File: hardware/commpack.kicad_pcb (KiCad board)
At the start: 2 copper layers, 103.8 x 62.5 mm, 11 parts, among them J1 1240COMM, J2 1240COMM_EXT, J3 L8BE-1G1T-91A

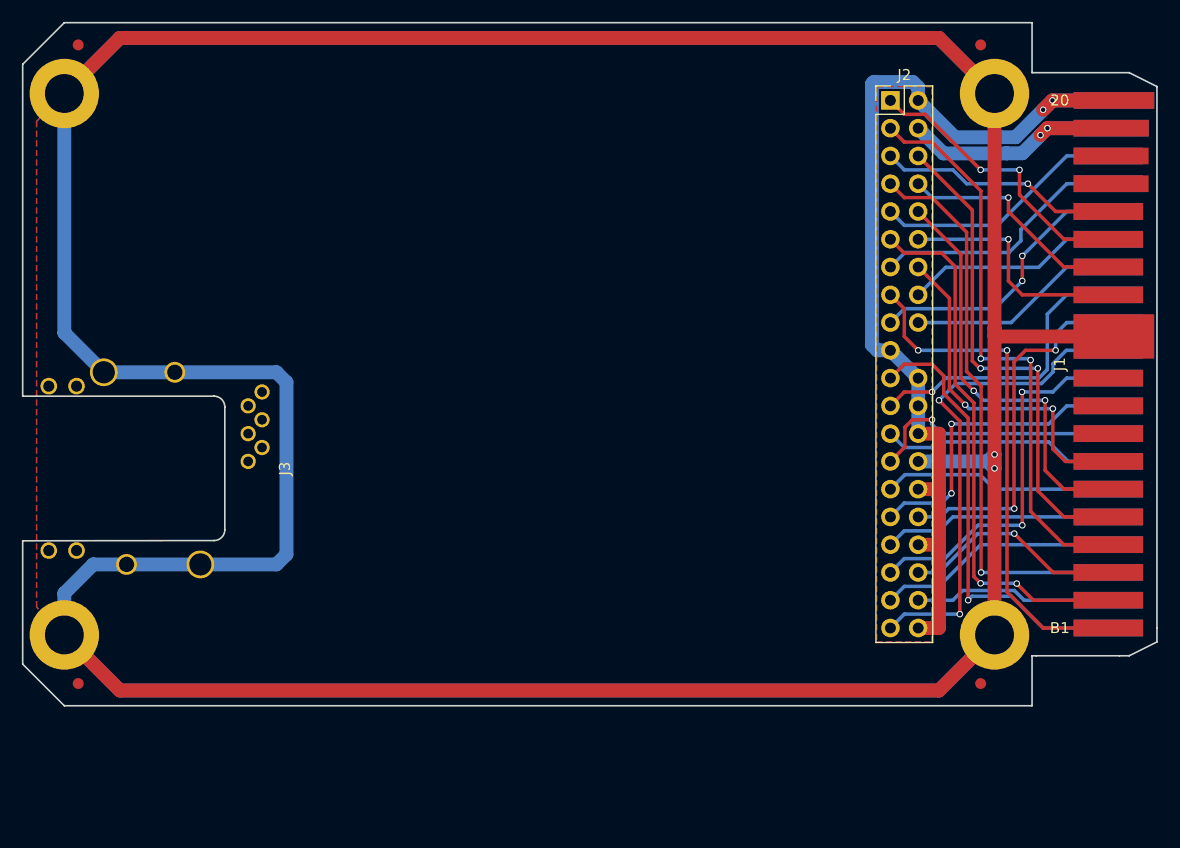
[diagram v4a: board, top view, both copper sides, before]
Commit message: Place UART and ROM, route data bus.
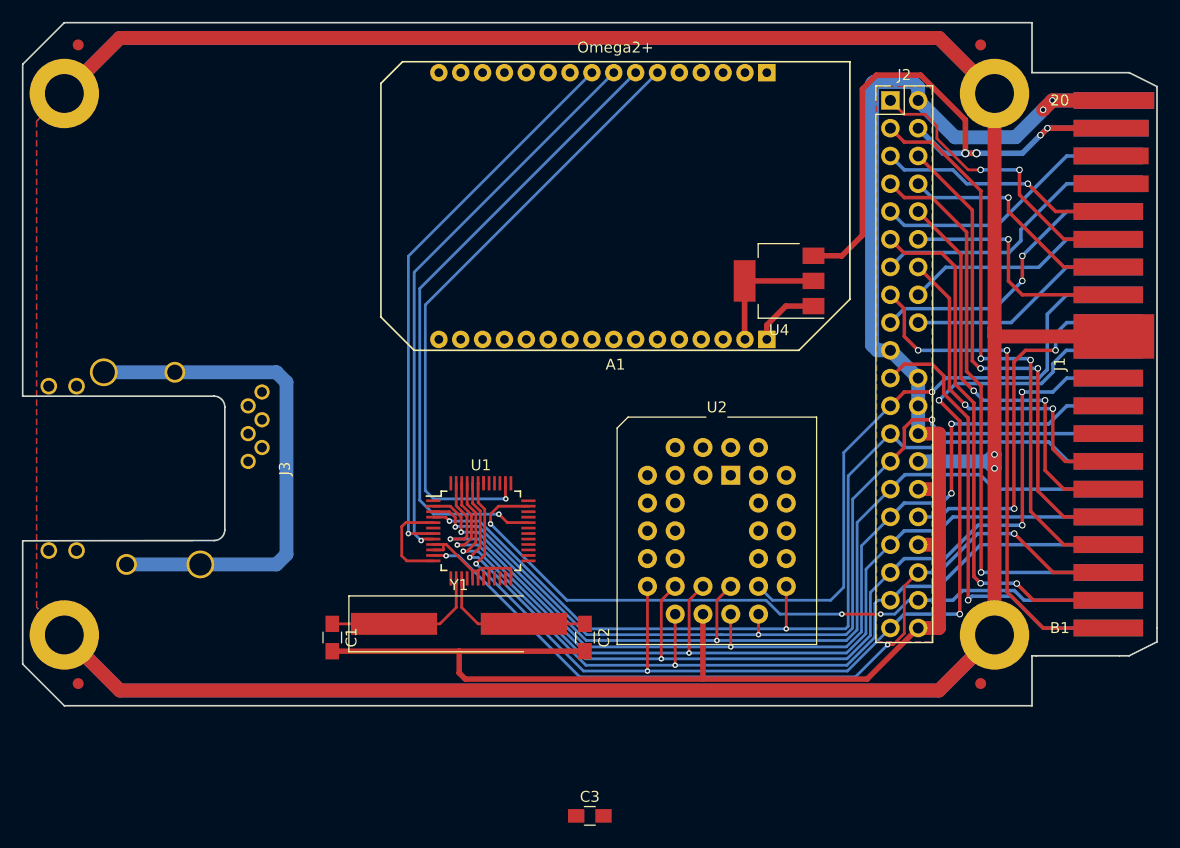
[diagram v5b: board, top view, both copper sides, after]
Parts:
- added A1: Omega2+, ether1240:Omega2, F.Cu at (176.1, 74.4)
- added C1: 22u, Capacitors_SMD:C_0805_HandSoldering, F.Cu at (150.2, 113.9)
- added C2: 22u, Capacitors_SMD:C_0805_HandSoldering, F.Cu at (173.4, 113.9)
- added C3: 22u, Capacitors_SMD:C_0805_HandSoldering, F.Cu at (173.8, 130.2)
- added U1: SC16C550B, Housings_QFP:LQFP-48_7x7mm_Pitch0.5mm, F.Cu at (163.8, 104.1)
- added U2: SST39SF010A, ether1240:PLCC-32_THT-Socket, F.Cu at (186.7, 99.1)
- added U4: AP1117-33, TO_SOT_Packages_SMD:SOT-223-3_TabPin2, F.Cu at (191.1, 81.3)
- added Y1: Crystal, Crystals:Crystal_SMD_HC49-SD_HandSoldering, F.Cu at (161.8, 112.6)
- J1: footprint 1240COMM -> ether1240:1240COMM
- J3: footprint L8BE-1G1T-91A -> ether1240:L8BE-1G1T-91A
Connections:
- net +5V renamed VCC
- net Net-(J1-PadA12) renamed /H-FREQ
- J1 pad B10: Net-(J1-PadB10) -> (no net)
- J1 pad B17: Net-(J1-PadB17) -> (no net)
- J1 pad B18: Net-(J1-PadB18) -> (no net)
- J1 pad B8: Net-(J1-PadB8) -> (no net)
- J1 pad B9: Net-(J1-PadB9) -> (no net)
- J3 pad 11: Net-(J3-Pad11) -> (no net)
- J3 pad 5: Net-(J3-Pad5) -> (no net)
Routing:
- net GND: track 85.7 -> 180.6 mm
- net /H-D7: track 18.2 -> 83.6 mm, vias 0 -> 2
- net /H-D3: track 17.8 -> 82.7 mm, vias 0 -> 2
- net /H-D5: track 17.9 -> 82.6 mm, vias 0 -> 2
- net /H-D4: track 24.7 -> 88.4 mm, vias 2 -> 4
- net /H-D2: track 31.3 -> 94.4 mm, vias 2 -> 4
- net /H-D6: track 20.2 -> 82.5 mm, vias 1 -> 3
- net /H-D0: track 41.9 -> 101.2 mm, vias 2 -> 4
- net /H-D1: track 18.9 -> 77.9 mm, vias 0 -> 2
- net /A-~CTS: track 0.00 -> 58.1 mm, vias 0 -> 1
- net /A-~RTS: track 0.00 -> 56.2 mm, vias 0 -> 1
- net /H-~CS: track 17.2 -> 73.2 mm, vias 1 -> 3
- net /A-RX: track 0.00 -> 51.8 mm, vias 0 -> 1
- net /A-TX: track 0.00 -> 51.4 mm, vias 0 -> 1
- net /H-RST: track 15.0 -> 63.3 mm, vias 0 -> 3
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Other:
- net class Default: clearance 0.2 -> 0.1524; trace_width 0.32258 -> 0.254; via_dia 0.6 -> 0.508; via_drill 0.4 -> 0.254
- net class Power: clearance 0.2 -> 0.1524; trace_width 1.27 -> 0.508; via_dia 0.6 -> 0.762; via_drill 0.4 -> 0.508
- rule trace_clearance: 0.2 -> 0.1524

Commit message: Route the remaining signals.
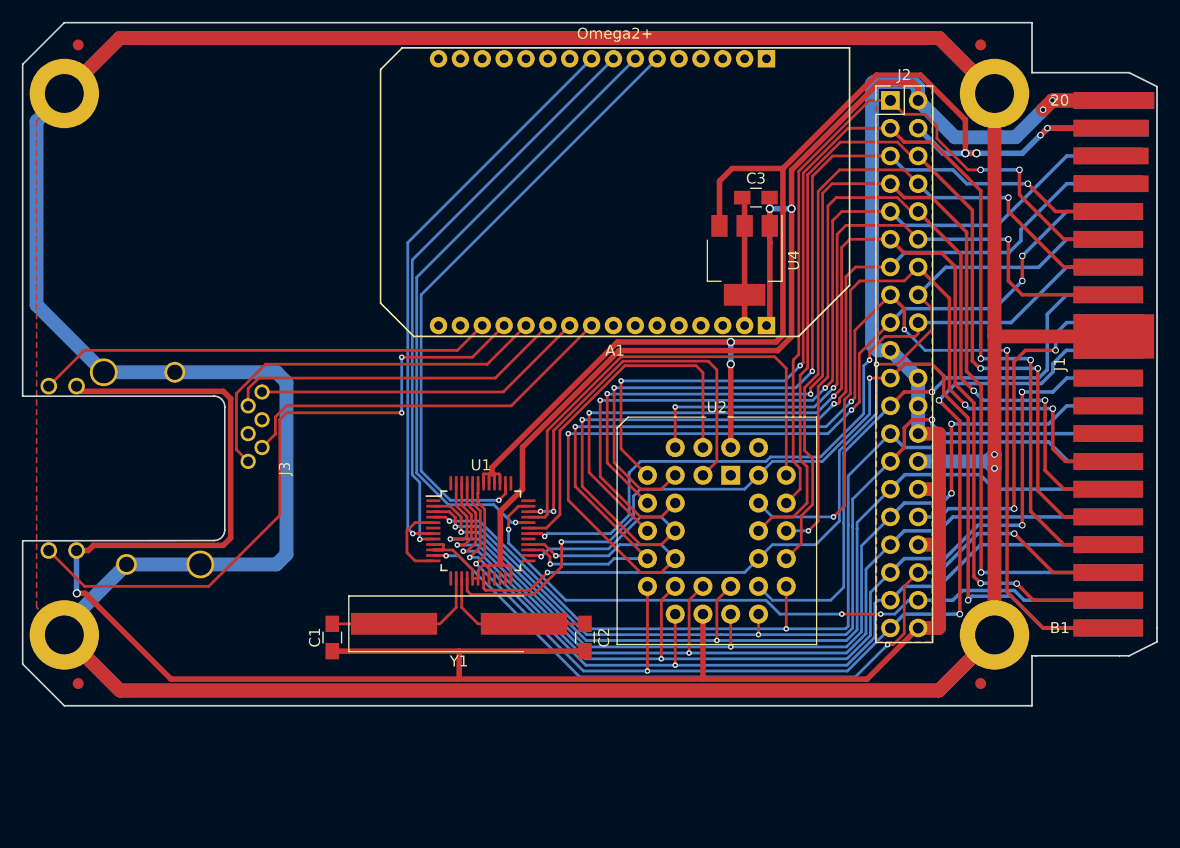
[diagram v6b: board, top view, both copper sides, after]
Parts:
- moved C3 58.6 mm to (189.0, 73.7)
- moved U4 3.67 mm to (188.0, 79.4), turned to 270 degrees
- moved A1 1.27 mm to (176.1, 73.2)
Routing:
- net GND: track 180.6 -> 345.6 mm, vias 2 -> 5
- net /H-A2: track 20.5 -> 93.7 mm, vias 0 -> 3
- net /H-A0: track 22.3 -> 92.5 mm, vias 2 -> 5
- net VCC: track 54.3 -> 118.3 mm, vias 4 -> 6
- net /H-A1: track 43.8 -> 107.7 mm, vias 2 -> 5
- net /H-~RD: track 16.3 -> 78.3 mm, vias 0 -> 2
- net Net-(A1-PadB13): track 0.00 -> 61.0 mm, vias 0 -> 2
- net /H-A6: track 18.9 -> 77.3 mm, vias 1 -> 3
- net /H-A4: track 19.9 -> 78.1 mm, vias 0 -> 2
- net /H-A5: track 49.0 -> 104.5 mm, vias 1 -> 3
- net /H-A3: track 46.0 -> 100.7 mm, vias 2 -> 4
- net /H-A7: track 49.6 -> 103.7 mm, vias 2 -> 4
- net /H-~WR: track 38.3 -> 90.9 mm, vias 1 -> 3
- net /H-INT: track 16.3 -> 66.1 mm, vias 0 -> 2
- net /H-A9: track 42.5 -> 91.1 mm
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
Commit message: Fix up rear silkscreen.
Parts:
- added Bonsai: Bonsai, ether1240:Bonsai, F.Cu at (155.6, 104.1)
- added G***: LOGO, ether1240:OSHW, B.Cu at (170.2, 102.9)

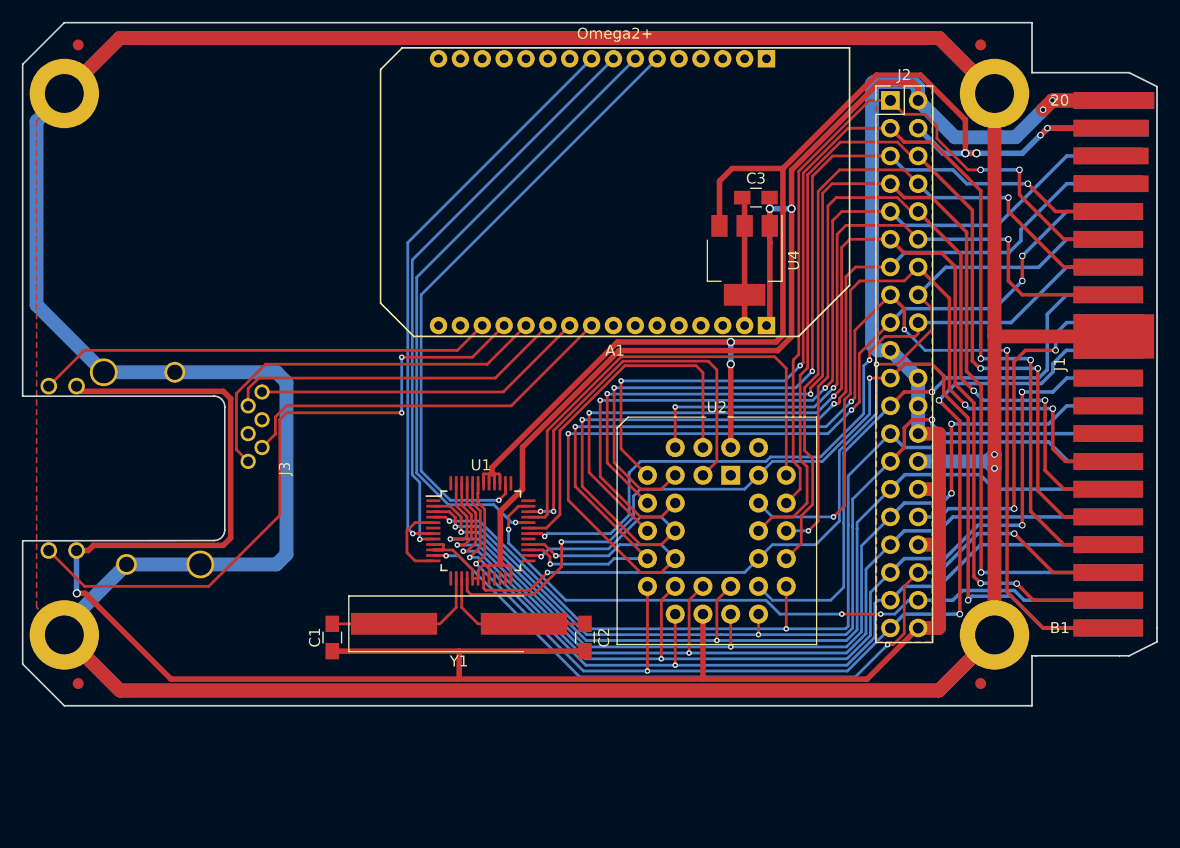
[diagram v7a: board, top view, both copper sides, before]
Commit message: Add decoupling caps on UART and ROM.
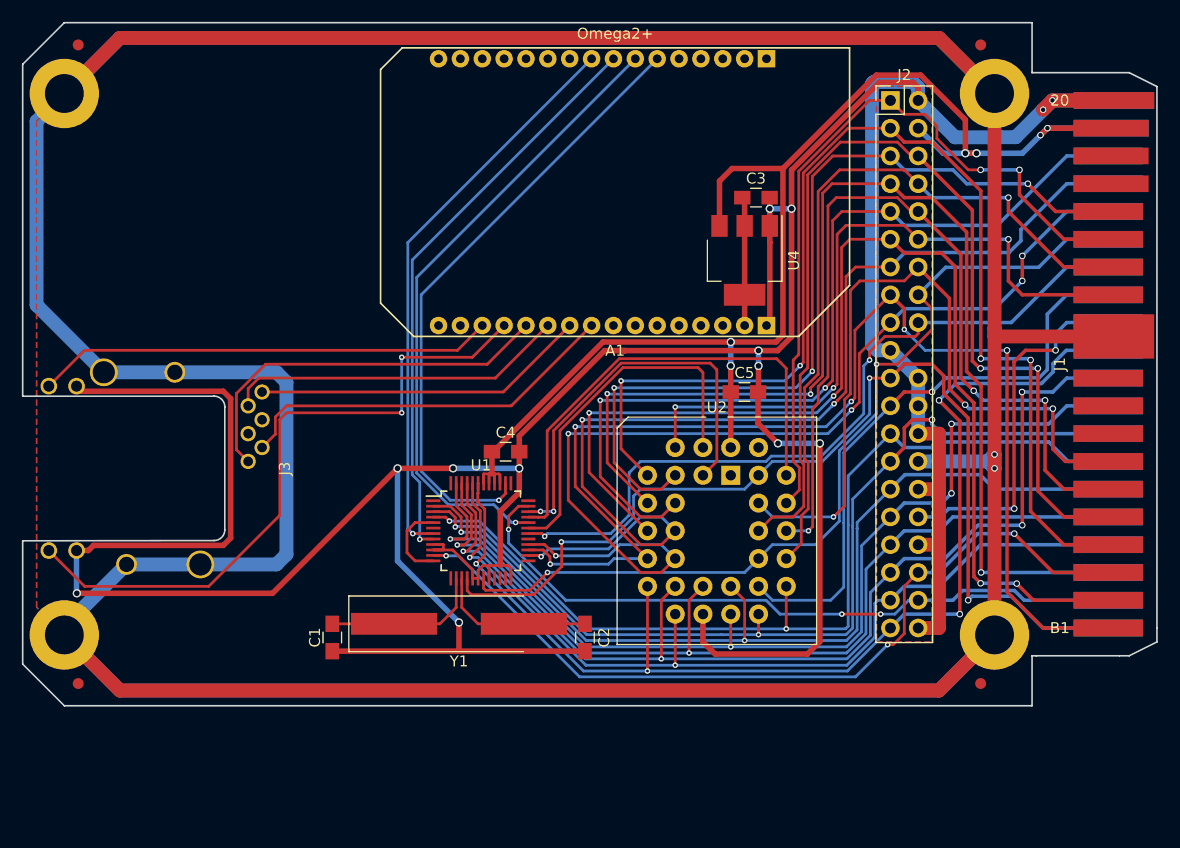
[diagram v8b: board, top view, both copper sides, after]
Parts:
- added C4: 22u, Capacitors_SMD:C_0805_HandSoldering, F.Cu at (166.1, 96.9)
- added C5: 22u, Capacitors_SMD:C_0805_HandSoldering, F.Cu at (187.9, 91.4)
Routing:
- net GND: track 345.6 -> 366.0 mm, vias 5 -> 13
- net VCC: track 118.3 -> 119.2 mm
